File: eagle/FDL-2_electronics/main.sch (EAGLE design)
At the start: 10 parts

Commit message: some changes
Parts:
- removed SV1: (no value), con-lstb:MA04-1
- added SV3: (no value), con-lstb:MA05-1
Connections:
- net N$17: now also SV3.4; no longer SV1.4
- net N$18: now also SV3.3; no longer SV1.3
- net N$19: now also SV3.2; no longer SV1.2
- net N$2: now also SV3.5
- net N$20: now also SV3.1; no longer SV1.1
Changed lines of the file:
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@@
 <part name="FIRE" library="con-lstb" deviceset="MA03-1" device="" value=""/>
 <part name="U$1" library="con-lstb" deviceset="MA03-1" device=""/>
-<part name="SV1" library="con-lstb" deviceset="MA04-1" device="" package3d_urn="urn:adsk.eagle:package:8337/1"/>
+<part name="SV3" library="con-lstb" deviceset="MA05-1" device="" package3d_urn="urn:adsk.eagle:package:8332/1"/>
 </parts>
 <sheets>
@@
 <instance part="FIRE" gate="G$1" x="-10.16" y="45.72" rot="MR0"/>
 <instance part="U$1" gate="G$1" x="73.66" y="86.36" rot="R180"/>
-<instance part="SV1" gate="1" x="78.74" y="20.32" rot="MR0"/>
+<instance part="SV3" gate="G$1" x="73.66" y="20.32" rot="MR0"/>
 </instances>
 <busses>
@@
 <pinref part="B1" gate="G$1" pin="*9"/>
 <wire x1="7.62" y1="45.72" x2="5.08" y2="45.72" width="0.1524" layer="91"/>
+<wire x1="5.08" y1="45.72" x2="5.08" y2="25.4" width="0.1524" layer="91"/>
+<pinref part="SV3" gate="G$1" pin="5"/>
+<wire x1="5.08" y1="25.4" x2="66.04" y2="25.4" width="0.1524" layer="91"/>
 </segment>
 </net>
@@
 <wire x1="30.48" y1="50.8" x2="43.18" y2="50.8" width="0.1524" layer="91"/>
 <wire x1="43.18" y1="50.8" x2="43.18" y2="20.32" width="0.1524" layer="91"/>
-<pinref part="SV1" gate="1" pin="3"/>
-<wire x1="43.18" y1="20.32" x2="71.12" y2="20.32" width="0.1524" layer="91"/>
+<pinref part="SV3" gate="G$1" pin="3"/>
+<wire x1="43.18" y1="20.32" x2="66.04" y2="20.32" width="0.1524" layer="91"/>
 </segment>
 </net>
@@
 <wire x1="30.48" y1="53.34" x2="45.72" y2="53.34" width="0.1524" layer="91"/>
 <wire x1="45.72" y1="53.34" x2="45.72" y2="22.86" width="0.1524" layer="91"/>
-<pinref part="SV1" gate="1" pin="4"/>
-<wire x1="71.12" y1="22.86" x2="45.72" y2="22.86" width="0.1524" layer="91"/>
+<pinref part="SV3" gate="G$1" pin="4"/>
+<wire x1="45.72" y1="22.86" x2="66.04" y2="22.86" width="0.1524" layer="91"/>
 </segment>
 </net>
@@
 <wire x1="30.48" y1="48.26" x2="40.64" y2="48.26" width="0.1524" layer="91"/>
 <wire x1="40.64" y1="48.26" x2="40.64" y2="17.78" width="0.1524" layer="91"/>
-<pinref part="SV1" gate="1" pin="2"/>
-<wire x1="40.64" y1="17.78" x2="71.12" y2="17.78" width="0.1524" layer="91"/>
+<pinref part="SV3" gate="G$1" pin="2"/>
+<wire x1="40.64" y1="17.78" x2="66.04" y2="17.78" width="0.1524" layer="91"/>
 </segment>
 </net>
@@
 <wire x1="30.48" y1="45.72" x2="38.1" y2="45.72" width="0.1524" layer="91"/>
 <wire x1="38.1" y1="45.72" x2="38.1" y2="15.24" width="0.1524" layer="91"/>
-<pinref part="SV1" gate="1" pin="1"/>
-<wire x1="38.1" y1="15.24" x2="71.12" y2="15.24" width="0.1524" layer="91"/>
-</segment>
-</net>
+<pinref part="SV3" gate="G$1" pin="1"/>
+<wire x1="38.1" y1="15.24" x2="66.04" y2="15.24" width="0.1524" layer="91"/>
+</segment>
+</net>

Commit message: some update
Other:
- note added: "AI1"
- note added: "AI2"
- note added: "ESC"
- note added: "PWM"
- note added: "STBY"
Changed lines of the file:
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@@
 <grid distance="0.1" unitdist="inch" unit="inch" style="lines" multiple="1" display="no" altdistance="0.01" altunitdist="inch" altunit="inch"/>
 <layers>
-<layer number="1" name="Top" color="4" fill="1" visible="no" active="no"/>
-<layer number="16" name="Bottom" color="1" fill="1" visible="no" active="no"/>
-<layer number="17" name="Pads" color="2" fill="1" visible="no" active="no"/>
-<layer number="18" name="Vias" color="2" fill="1" visible="no" active="no"/>
-<layer number="19" name="Unrouted" color="6" fill="1" visible="no" active="no"/>
-<layer number="20" name="Dimension" color="24" fill="1" visible="no" active="no"/>
-<layer number="21" name="tPlace" color="7" fill="1" visible="no" active="no"/>
-<layer number="22" name="bPlace" color="7" fill="1" visible="no" active="no"/>
-<layer number="23" name="tOrigins" color="15" fill="1" visible="no" active="no"/>
-<layer number="24" name="bOrigins" color="15" fill="1" visible="no" active="no"/>
-<layer number="25" name="tNames" color="7" fill="1" visible="no" active="no"/>
-<layer number="26" name="bNames" color="7" fill="1" visible="no" active="no"/>
-<layer number="27" name="tValues" color="7" fill="1" visible="no" active="no"/>
-<layer number="28" name="bValues" color="7" fill="1" visible="no" active="no"/>
+<layer number="1" name="Top" color="4" fill="1" visible="yes" active="no"/>
+<layer number="16" name="Bottom" color="1" fill="1" visible="yes" active="no"/>
+<layer number="17" name="Pads" color="2" fill="1" visible="yes" active="no"/>
+<layer number="18" name="Vias" color="2" fill="1" visible="yes" active="no"/>
+<layer number="19" name="Unrouted" color="6" fill="1" visible="yes" active="no"/>
+<layer number="20" name="Dimension" color="24" fill="1" visible="yes" active="no"/>
+<layer number="21" name="tPlace" color="7" fill="1" visible="yes" active="no"/>
+<layer number="22" name="bPlace" color="7" fill="1" visible="yes" active="no"/>
+<layer number="23" name="tOrigins" color="15" fill="1" visible="yes" active="no"/>
+<layer number="24" name="bOrigins" color="15" fill="1" visible="yes" active="no"/>
+<layer number="25" name="tNames" color="7" fill="1" visible="yes" active="no"/>
+<layer number="26" name="bNames" color="7" fill="1" visible="yes" active="no"/>
+<layer number="27" name="tValues" color="7" fill="1" visible="yes" active="no"/>
+<layer number="28" name="bValues" color="7" fill="1" visible="yes" active="no"/>
 <layer number="29" name="tStop" color="7" fill="3" visible="no" active="no"/>
 <layer number="30" name="bStop" color="7" fill="6" visible="no" active="no"/>
@@
 <layer number="35" name="tGlue" color="7" fill="4" visible="no" active="no"/>
 <layer number="36" name="bGlue" color="7" fill="5" visible="no" active="no"/>
-<layer number="37" name="tTest" color="7" fill="1" visible="no" active="no"/>
-<layer number="38" name="bTest" color="7" fill="1" visible="no" active="no"/>
+<layer number="37" name="tTest" color="7" fill="1" visible="yes" active="no"/>
+<layer number="38" name="bTest" color="7" fill="1" visible="yes" active="no"/>
 <layer number="39" name="tKeepout" color="4" fill="11" visible="no" active="no"/>
 <layer number="40" name="bKeepout" color="1" fill="11" visible="no" active="no"/>
@@
 <layer number="44" name="Drills" color="7" fill="1" visible="no" active="no"/>
 <layer number="45" name="Holes" color="7" fill="1" visible="no" active="no"/>
-<layer number="46" name="Milling" color="3" fill="1" visible="no" active="no"/>
-<layer number="47" name="Measures" color="7" fill="1" visible="no" active="no"/>
-<layer number="48" name="Document" color="7" fill="1" visible="no" active="no"/>
-<layer number="49" name="Reference" color="7" fill="1" visible="no" active="no"/>
-<layer number="50" name="dxf" color="7" fill="1" visible="no" active="no"/>
-<layer number="51" name="tDocu" color="7" fill="1" visible="no" active="no"/>
-<layer number="52" name="bDocu" color="7" fill="1" visible="no" active="no"/>
-<layer number="53" name="tGND_GNDA" color="7" fill="9" visible="no" active="no"/>
-<layer number="54" name="bGND_GNDA" color="1" fill="9" visible="no" active="no"/>
-<layer number="56" name="wert" color="7" fill="1" visible="no" active="no"/>
-<layer number="57" name="tCAD" color="7" fill="1" visible="no" active="no"/>
-<layer number="59" name="tCarbon" color="7" fill="1" visible="no" active="no"/>
-<layer number="60" name="bCarbon" color="7" fill="1" visible="no" active="no"/>
+<layer number="46" name="Milling" color="3" fill="1" visible="yes" active="no"/>
+<layer number="47" name="Measures" color="7" fill="1" visible="yes" active="no"/>
+<layer number="48" name="Document" color="7" fill="1" visible="yes" active="no"/>
+<layer number="49" name="Reference" color="7" fill="1" visible="yes" active="no"/>
+<layer number="50" name="dxf" color="7" fill="1" visible="yes" active="no"/>
+<layer number="51" name="tDocu" color="7" fill="1" visible="yes" active="no"/>
+<layer number="52" name="bDocu" color="7" fill="1" visible="yes" active="no"/>
+<layer number="53" name="tGND_GNDA" color="7" fill="9" visible="yes" active="no"/>
+<layer number="54" name="bGND_GNDA" color="1" fill="9" visible="yes" active="no"/>
+<layer number="56" name="wert" color="7" fill="1" visible="yes" active="no"/>
+<layer number="57" name="tCAD" color="7" fill="1" visible="yes" active="no"/>
+<layer number="59" name="tCarbon" color="7" fill="1" visible="yes" active="no"/>
+<layer number="60" name="bCarbon" color="7" fill="1" visible="yes" active="no"/>
 <layer number="88" name="SimResults" color="9" fill="1" visible="yes" active="yes"/>
 <layer number="89" name="SimProbes" color="9" fill="1" visible="yes" active="yes"/>
@@
 <sheet>
 <plain>
+<text x="78.74" y="15.24" size="1.4224" layer="91">ESC</text>
+<text x="78.74" y="17.78" size="1.4224" layer="91">PWM</text>
+<text x="78.74" y="20.32" size="1.4224" layer="91">AI2</text>
+<text x="78.74" y="22.86" size="1.4224" layer="91">AI1</text>
+<text x="78.74" y="25.4" size="1.4224" layer="91">STBY</text>
 </plain>
 <instances>

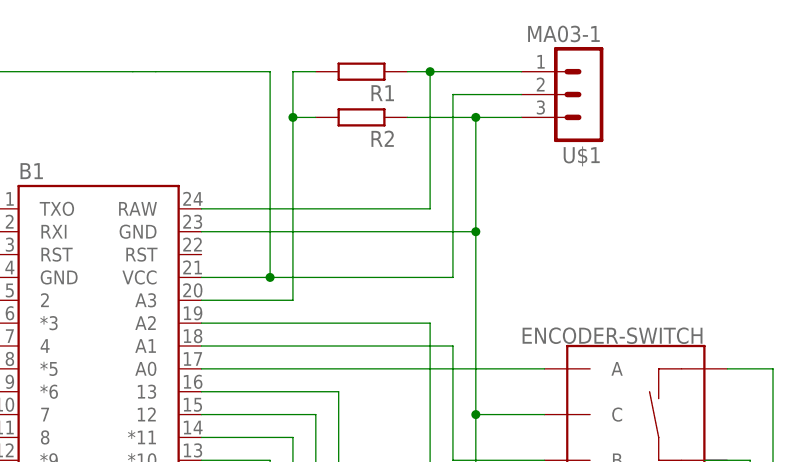
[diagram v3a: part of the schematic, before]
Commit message: update resistors
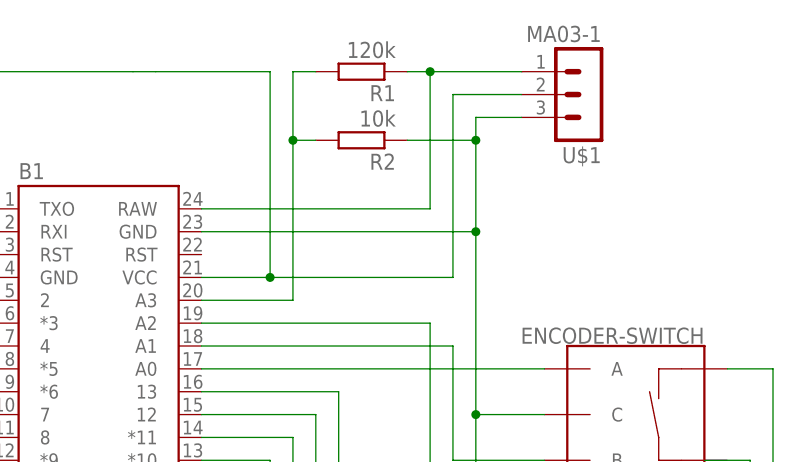
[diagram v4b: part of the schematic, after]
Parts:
- R1: value (none) -> 120k
- R2: value (none) -> 10k
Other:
- moved on the sheet: R2
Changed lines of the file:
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@@
 <?xml version="1.0" encoding="utf-8"?>
 <!DOCTYPE eagle SYSTEM "eagle.dtd">
-<eagle version="8.5.0">
+<eagle version="9.0.0">
 <drawing>
 <settings>
@@
 <part name="P-FRONT" library="con-lstb" deviceset="MA02-1" device=""/>
 <part name="S1" library="SparkFun-Switches" deviceset="ENCODER-SWITCH" device=""/>
-<part name="R1" library="rcl" library_urn="urn:adsk.eagle:library:334" deviceset="R-EU_" device="0204/5" package3d_urn="urn:adsk.eagle:package:23488/1"/>
-<part name="R2" library="rcl" library_urn="urn:adsk.eagle:library:334" deviceset="R-EU_" device="0204/2V" package3d_urn="urn:adsk.eagle:package:23495/1"/>
+<part name="R1" library="rcl" library_urn="urn:adsk.eagle:library:334" deviceset="R-EU_" device="0204/5" package3d_urn="urn:adsk.eagle:package:23488/1" value="120k"/>
+<part name="R2" library="rcl" library_urn="urn:adsk.eagle:library:334" deviceset="R-EU_" device="0204/2V" package3d_urn="urn:adsk.eagle:package:23495/1" value="10k"/>
 <part name="SV2" library="con-lstb" deviceset="MA04-1" device="" package3d_urn="urn:adsk.eagle:package:8337/1"/>
 <part name="FIRE" library="con-lstb" deviceset="MA03-1" device="" value=""/>
@@
 <instance part="S1" gate="G$1" x="78.74" y="50.8" rot="R180"/>
 <instance part="R1" gate="G$1" x="48.26" y="88.9" rot="R180"/>
-<instance part="R2" gate="G$1" x="48.26" y="83.82" rot="R180"/>
+<instance part="R2" gate="G$1" x="48.26" y="81.28" rot="R180"/>
 <instance part="SV2" gate="1" x="-10.16" y="-5.08" rot="MR0"/>
 <instance part="FIRE" gate="G$1" x="-10.16" y="45.72" rot="MR0"/>
@@
 <net name="N$12" class="0">
 <segment>
-<wire x1="60.96" y1="83.82" x2="60.96" y2="71.12" width="0.1524" layer="91"/>
+<wire x1="60.96" y1="81.28" x2="60.96" y2="71.12" width="0.1524" layer="91"/>
 <pinref part="B1" gate="G$1" pin="GND@2"/>
 <wire x1="60.96" y1="40.64" x2="60.96" y2="50.8" width="0.1524" layer="91"/>
@@
 <junction x="60.96" y="50.8"/>
 <pinref part="R2" gate="G$1" pin="1"/>
-<wire x1="53.34" y1="83.82" x2="60.96" y2="83.82" width="0.1524" layer="91"/>
+<wire x1="53.34" y1="81.28" x2="60.96" y2="81.28" width="0.1524" layer="91"/>
 <pinref part="U$1" gate="G$1" pin="3"/>
-<wire x1="60.96" y1="83.82" x2="66.04" y2="83.82" width="0.1524" layer="91"/>
-<junction x="60.96" y="83.82"/>
+<junction x="60.96" y="81.28"/>
 <wire x1="91.44" y1="40.64" x2="91.44" y2="45.72" width="0.1524" layer="91"/>
 <wire x1="91.44" y1="45.72" x2="86.36" y2="45.72" width="0.1524" layer="91"/>
+<wire x1="66.04" y1="83.82" x2="60.96" y2="83.82" width="0.1524" layer="91"/>
+<wire x1="60.96" y1="83.82" x2="60.96" y2="81.28" width="0.1524" layer="91"/>
 </segment>
 </net>
@@
 <segment>
 <pinref part="B1" gate="G$1" pin="A3"/>
-<wire x1="40.64" y1="88.9" x2="40.64" y2="83.82" width="0.1524" layer="91"/>
-<wire x1="40.64" y1="83.82" x2="40.64" y2="63.5" width="0.1524" layer="91"/>
+<wire x1="40.64" y1="88.9" x2="40.64" y2="81.28" width="0.1524" layer="91"/>
+<wire x1="40.64" y1="81.28" x2="40.64" y2="63.5" width="0.1524" layer="91"/>
 <wire x1="40.64" y1="63.5" x2="30.48" y2="63.5" width="0.1524" layer="91"/>
 <pinref part="R1" gate="G$1" pin="2"/>
 <wire x1="40.64" y1="88.9" x2="43.18" y2="88.9" width="0.1524" layer="91"/>
 <pinref part="R2" gate="G$1" pin="2"/>
-<wire x1="43.18" y1="83.82" x2="40.64" y2="83.82" width="0.1524" layer="91"/>
-<junction x="40.64" y="83.82"/>
-</segment>
-</net>
+<wire x1="43.18" y1="81.28" x2="40.64" y2="81.28" width="0.1524" layer="91"/>
+<junction x="40.64" y="81.28"/>
+</segment>
+</net>
